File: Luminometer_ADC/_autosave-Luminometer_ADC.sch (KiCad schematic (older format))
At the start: 71 parts, among them J1 Harting__15210122401000, U1 LT3464, U2 ADA4522-1, U3 ADR512, U4 ADR512, U5 ADA4522-4, U6 LP5907MFX-3, U7 ADS131M08IPBS

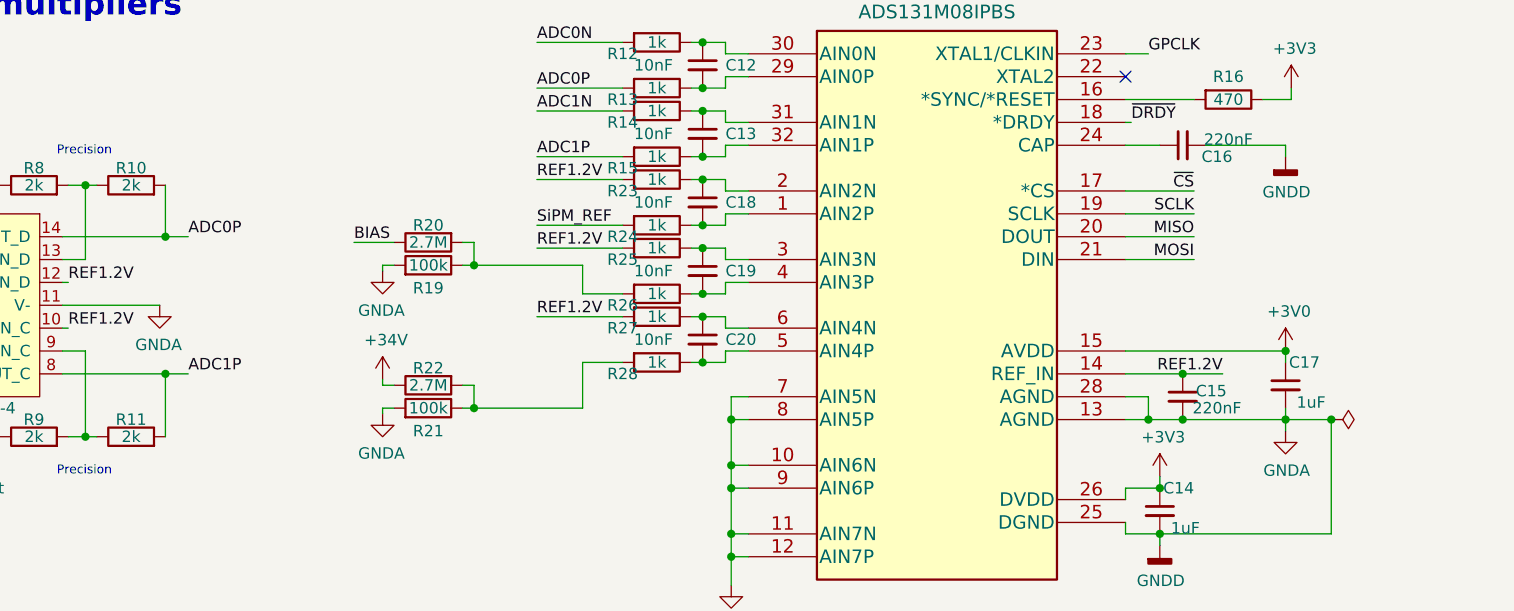
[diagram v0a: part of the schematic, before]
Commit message: Update ADC board
- Add ADC measurements for SiPM_REF, +34V, and BIAS for monitoring board
- Move differential amp lower on layout, to clear more space for shaft coupler
- Clean up routing
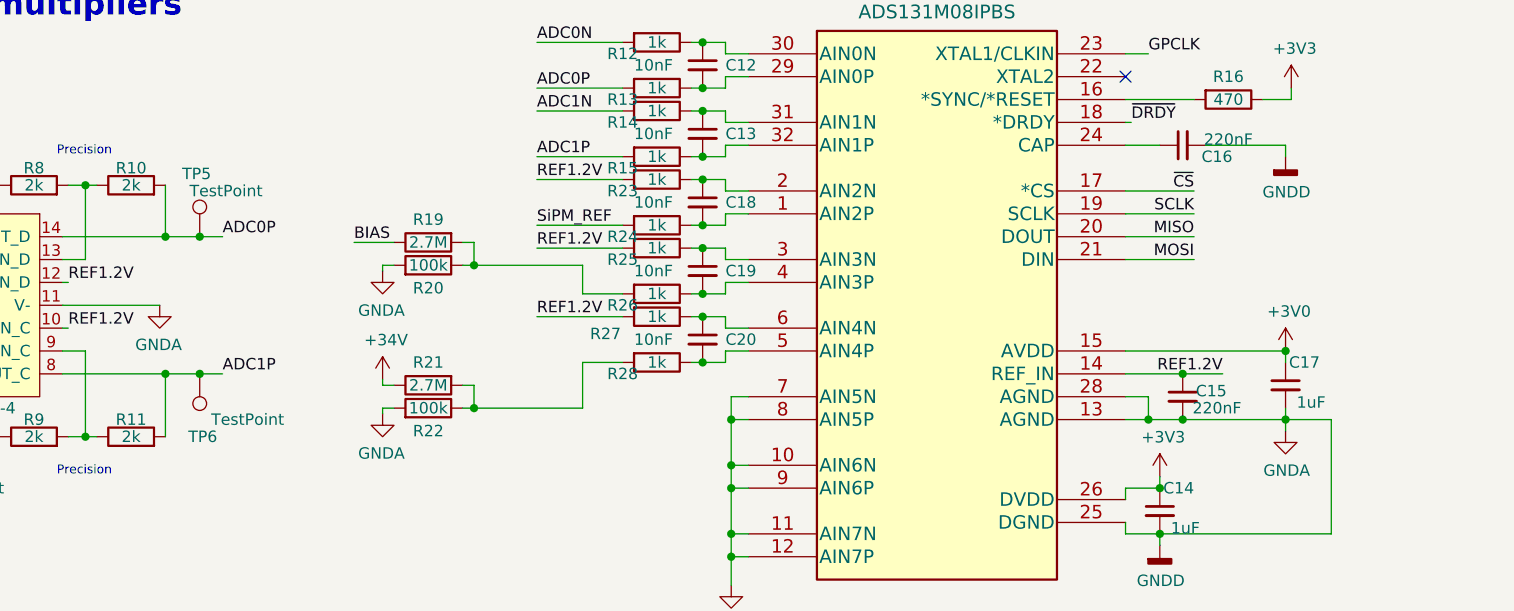
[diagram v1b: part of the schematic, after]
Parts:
- added TP5, TP6: TestPoint, TestPoint:TestPoint_Pad_1.0x1.0mm, symbol Connector:TestPoint
- TP3, TP4: footprint TestPoint:TestPoint_Pad_D1.5mm -> TestPoint:TestPoint_Pad_1.0x1.0mm
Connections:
- net ADC0P: now also TP5.1
- net ADC1P: now also TP6.1
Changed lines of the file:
@@
 	0    1    -1   0
 $EndComp
-Connection ~ 11000 3050
 $Comp
 L LuminometerCustomPartLib:MICROFC−60035−SMT SiPM1
@@
 	-1   0    0    -1
 $EndComp
-Text Label 6000 2250 0    50   ~ 0
+Text Label 6150 2250 0    50   ~ 0
 ADC0P
 Text Label 3750 1450 1    50   ~ 0
@@
 Wire Wire Line
 	5900 2850 5900 3125
-Text Label 6000 2850 0    50   ~ 0
+Text Label 6150 2850 0    50   ~ 0
 ADC1P
 Connection ~ 5900 2850
@@
 F 0 "TP4" H 4975 3450 50  0000 R CNN
 F 1 "TestPoint" H 4975 3350 50  0000 R CNN
-F 2 "TestPoint:TestPoint_Pad_D1.5mm" H 5125 3125 50  0001 C CNN
+F 2 "TestPoint:TestPoint_Pad_1.0x1.0mm" H 5125 3125 50  0001 C CNN
 F 3 "~" H 5125 3125 50  0001 C CNN
 	1    4925 3125
@@
 F 0 "TP3" H 4950 2300 50  0000 R CNN
 F 1 "TestPoint" H 5175 2225 50  0000 R CNN
-F 2 "TestPoint:TestPoint_Pad_D1.5mm" H 5100 2025 50  0001 C CNN
+F 2 "TestPoint:TestPoint_Pad_1.0x1.0mm" H 5100 2025 50  0001 C CNN
 F 3 "~" H 5100 2025 50  0001 C CNN
 	1    4900 2025
@@
 	0    -1   -1   0
 $EndComp
-$Comp
-L power:PWR_FLAG #FLG04
-U 1 1 5F65080C
-P 11000 3050
-F 0 "#FLG04" H 11000 3125 50  0001 C CNN
-F 1 "PWR_FLAG" V 11000 3177 50  0001 L CNN
-F 2 "" H 11000 3050 50  0001 C CNN
-F 3 "~" H 11000 3050 50  0001 C CNN
-	1    11000 3050
-	0    1    1    0
-$EndComp
 Wire Wire Line
 	7275 5450 7850 5450
@@
 	11000 3050 11000 3550
 Wire Wire Line
-	5900 2250 6000 2250
-Wire Wire Line
-	5900 2850 6000 2850
+	5900 2250 6050 2250
+Wire Wire Line
+	5900 2850 6050 2850
 $Comp
 L Connector:TestPoint TP2
@@
 U 1 1 60B19A67
 P 7050 2275
-F 0 "R19" V 7250 2275 50  0000 C CNN
+F 0 "R19" V 6950 2275 50  0000 C CNN
 F 1 "2.7M" V 7050 2275 50  0000 C CNN
 F 2 "Resistor_SMD:R_0603_1608Metric" V 6980 2275 50  0001 C CNN
@@
 U 1 1 60B19A74
 P 7050 2375
-F 0 "R20" V 7225 2375 50  0000 C CNN
+F 0 "R20" V 6950 2375 50  0000 C CNN
 F 1 "100k" V 7050 2375 50  0000 C CNN
 F 2 "Resistor_SMD:R_0603_1608Metric" V 6980 2375 50  0001 C CNN
@@
 U 1 1 6100066E
 P 8050 2600
-F 0 "R27" V 8100 2450 50  0000 C CNN
+F 0 "R27" V 8125 2375 50  0000 C CNN
 F 1 "1k" V 8050 2600 50  0000 C CNN
 F 2 "Resistor_SMD:R_0603_1608Metric" V 7980 2600 50  0001 C CNN
@@
 U 1 1 6110C7CE
 P 7050 2900
-F 0 "R21" V 7250 2900 50  0000 C CNN
+F 0 "R21" V 6950 2900 50  0000 C CNN
 F 1 "2.7M" V 7050 2900 50  0000 C CNN
 F 2 "Resistor_SMD:R_0603_1608Metric" V 6980 2900 50  0001 C CNN
@@
 U 1 1 6110C7DB
 P 7050 3000
-F 0 "R22" V 7225 3000 50  0000 C CNN
+F 0 "R22" V 6950 3000 50  0000 C CNN
 F 1 "100k" V 7050 3000 50  0000 C CNN
 F 2 "Resistor_SMD:R_0603_1608Metric" V 6980 3000 50  0001 C CNN
@@
 Wire Wire Line
 	7250 3000 7725 3000
+$Comp
+L Connector:TestPoint TP5
+U 1 1 612F5EA0
+P 6050 2250
+F 0 "TP5" H 6100 2525 50  0000 R CNN
+F 1 "TestPoint" H 6325 2450 50  0000 R CNN
+F 2 "TestPoint:TestPoint_Pad_1.0x1.0mm" H 6250 2250 50  0001 C CNN
+F 3 "~" H 6250 2250 50  0001 C CNN
+	1    6050 2250
+	1    0    0    -1
+$EndComp
+Connection ~ 6050 2250
+Wire Wire Line
+	6050 2250 6150 2250
+$Comp
+L Connector:TestPoint TP6
+U 1 1 612F6302
+P 6050 2850
+F 0 "TP6" H 6100 3125 50  0000 R CNN
+F 1 "TestPoint" H 6000 3050 50  0000 R CNN
+F 2 "TestPoint:TestPoint_Pad_1.0x1.0mm" H 6250 2850 50  0001 C CNN
+F 3 "~" H 6250 2850 50  0001 C CNN
+	1    6050 2850
+	-1   0    0    1
+$EndComp
+Connection ~ 6050 2850
+Wire Wire Line
+	6050 2850 6150 2850
 $EndSCHEMATC
